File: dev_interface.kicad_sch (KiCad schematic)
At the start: 0 parts

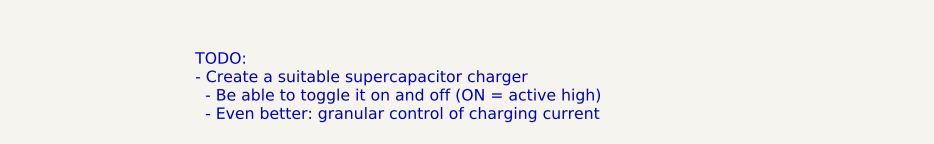
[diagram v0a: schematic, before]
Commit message: Added some text in the subsheets to outline what needs to be added inside of each subsheet
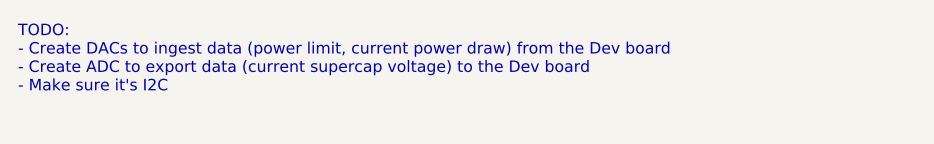
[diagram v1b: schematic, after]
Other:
- note added: "TODO: - Create DACs to ingest data (power limit, current power draw) from the Dev board - Create ADC to export data (current supercap voltage) to the Dev board - Make sure it's I2C"
- note removed: "TODO: - Create a suitable supercapacitor charger - Be able to toggle it on and off (ON = active high) - Even better: granular control of charging current"
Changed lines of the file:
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@@
 		(comment 1 "Robomaster")
 	)
-	(text "TODO:\n- Create a suitable supercapacitor charger\n  - Be able to toggle it on and off (ON = active high)\n  - Even better: granular control of charging current"
+	(text "TODO:\n- Create DACs to ingest data (power limit, current power draw) from the Dev board\n- Create ADC to export data (current supercap voltage) to the Dev board\n- Make sure it's I2C"
 		(exclude_from_sim no)
-		(at 132.08 95.25 0)
+		(at 112.395 92.075 0)
 		(effects
 			(font

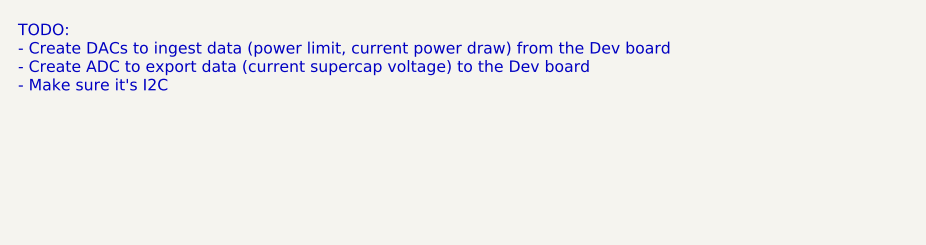
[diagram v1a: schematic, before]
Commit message: Added in & out data from each subsheet
For more details, please contact @leftisttachyon on Discord
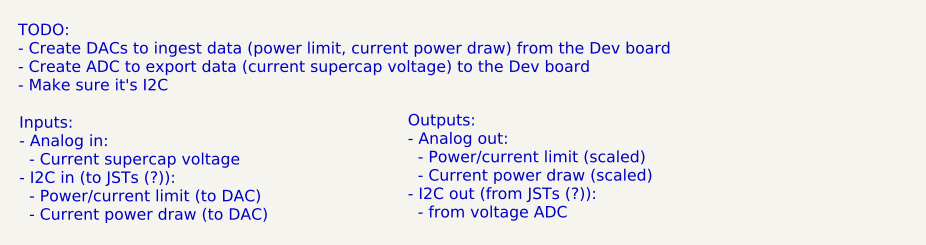
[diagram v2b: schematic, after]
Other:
- note added: "Inputs: - Analog in: - Current supercap voltage - I2C in (to JSTs (?)): - Power/current limit (to DAC) - Current power draw (to DAC)"
- note added: "Outputs: - Analog out: - Power/current limit (scaled) - Current power draw (scaled) - I2C out (from JSTs (?)): - from voltage ADC"
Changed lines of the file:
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@@
+		)
+	)
+	(text "Inputs:\n- Analog in:\n  - Current supercap voltage\n- I2C in (to JSTs (?)):\n  - Power/current limit (to DAC)\n  - Current power draw (to DAC)"
+		(exclude_from_sim no)
+		(at 112.522 102.362 0)
+		(effects
+			(font
+				(size 1.27 1.27)
+			)
+			(justify left top)
+		)
+	)
+	(text "Outputs:\n- Analog out:\n  - Power/current limit (scaled)\n  - Current power draw (scaled)\n- I2C out (from JSTs (?)):\n  - from voltage ADC"
+		(exclude_from_sim no)
+		(at 155.702 102.108 0)
+		(effects
+			(font
+				(size 1.27 1.27)
+			)
+			(justify left top)
 		)
 	)

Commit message: Completed first version of housekeeping supplies
+5V and +3V3 from mini PC +24V
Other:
- company: UT Stampede -> UT Robomaster
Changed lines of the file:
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@@
 	(paper "A4")
 	(title_block
-		(date "2024-10-18")
+		(date "2024-11-15")
 		(rev "1")
-		(company "UT Stampede")
+		(company "UT Robomaster")
 		(comment 1 "Robomaster")
 	)

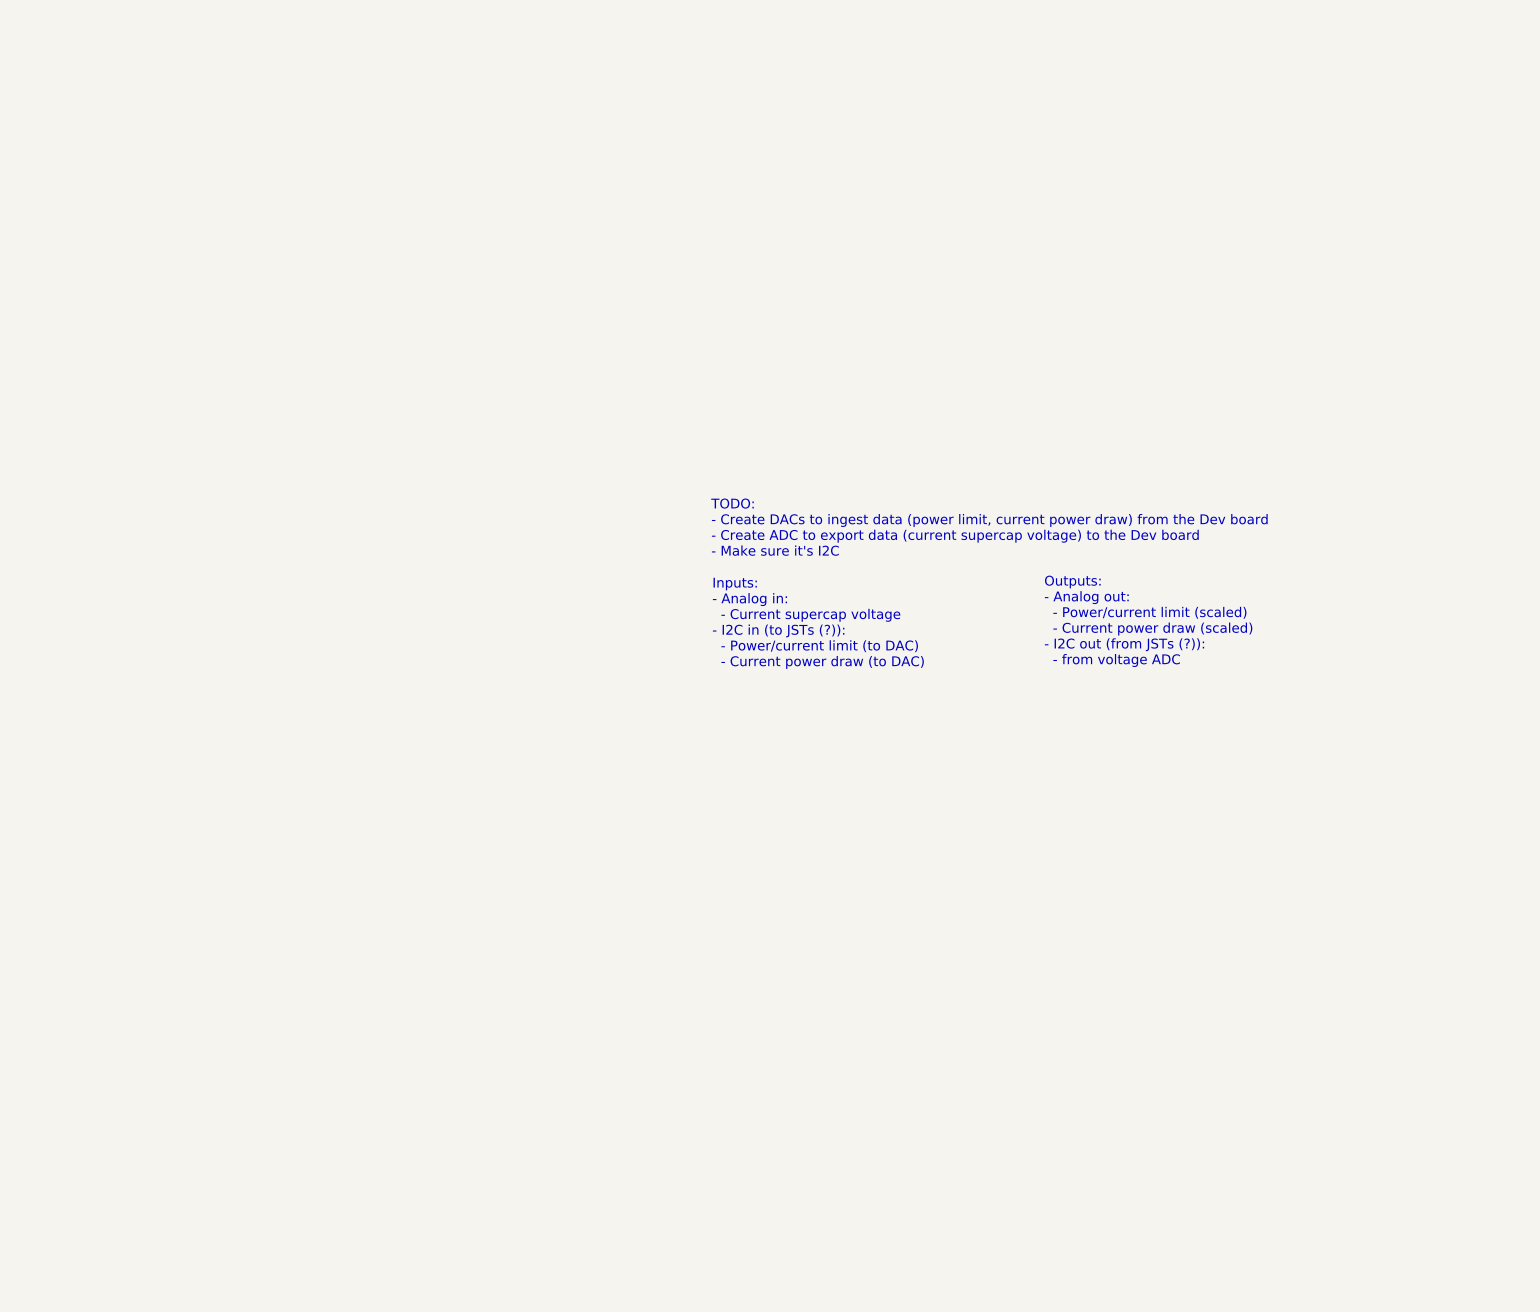
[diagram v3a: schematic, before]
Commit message: Selected an ideal diode
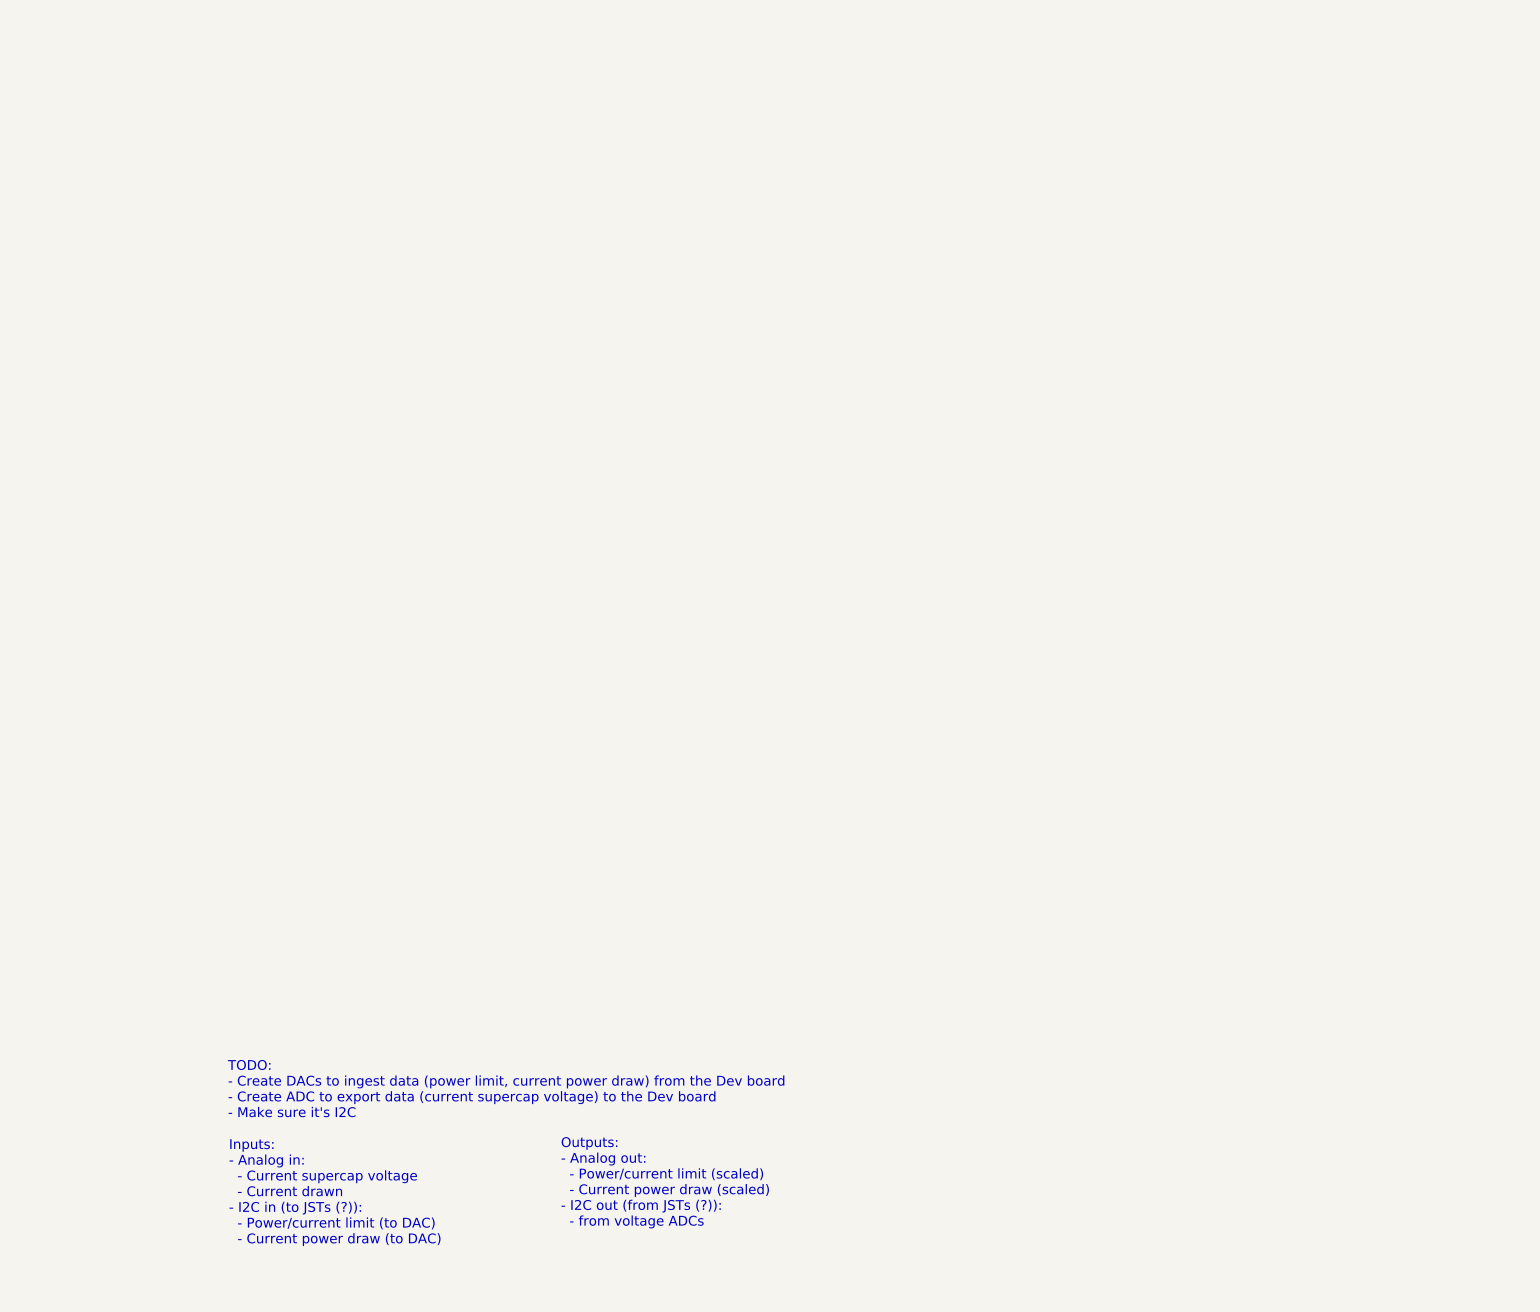
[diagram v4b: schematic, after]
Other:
- note added: "Inputs: - Analog in: - Current supercap voltage - Current drawn - I2C in (to JSTs (?)): - Power/current limit (to DAC) - Current power draw (to DAC)"
- note added: "Outputs: - Analog out: - Power/current limit (scaled) - Current power draw (scaled) - I2C out (from JSTs (?)): - from voltage ADCs"
- note removed: "Inputs: - Analog in: - Current supercap voltage - I2C in (to JSTs (?)): - Power/current limit (to DAC) - Current power draw (to DAC)"
- note removed: "Outputs: - Analog out: - Power/current limit (scaled) - Current power draw (scaled) - I2C out (from JSTs (?)): - from voltage ADC"
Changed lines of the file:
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@@
 	(text "TODO:\n- Create DACs to ingest data (power limit, current power draw) from the Dev board\n- Create ADC to export data (current supercap voltage) to the Dev board\n- Make sure it's I2C"
 		(exclude_from_sim no)
-		(at 112.395 92.075 0)
+		(at 49.53 165.1 0)
 		(effects
 			(font
@@
 		)
 	)
-	(text "Inputs:\n- Analog in:\n  - Current supercap voltage\n- I2C in (to JSTs (?)):\n  - Power/current limit (to DAC)\n  - Current power draw (to DAC)"
+	(text "Inputs:\n- Analog in:\n  - Current supercap voltage\n  - Current drawn\n- I2C in (to JSTs (?)):\n  - Power/current limit (to DAC)\n  - Current power draw (to DAC)"
 		(exclude_from_sim no)
-		(at 112.522 102.362 0)
+		(at 49.657 175.387 0)
 		(effects
 			(font
@@
 		)
 	)
-	(text "Outputs:\n- Analog out:\n  - Power/current limit (scaled)\n  - Current power draw (scaled)\n- I2C out (from JSTs (?)):\n  - from voltage ADC"
+	(text "Outputs:\n- Analog out:\n  - Power/current limit (scaled)\n  - Current power draw (scaled)\n- I2C out (from JSTs (?)):\n  - from voltage ADCs"
 		(exclude_from_sim no)
-		(at 155.702 102.108 0)
+		(at 92.837 175.133 0)
 		(effects
 			(font

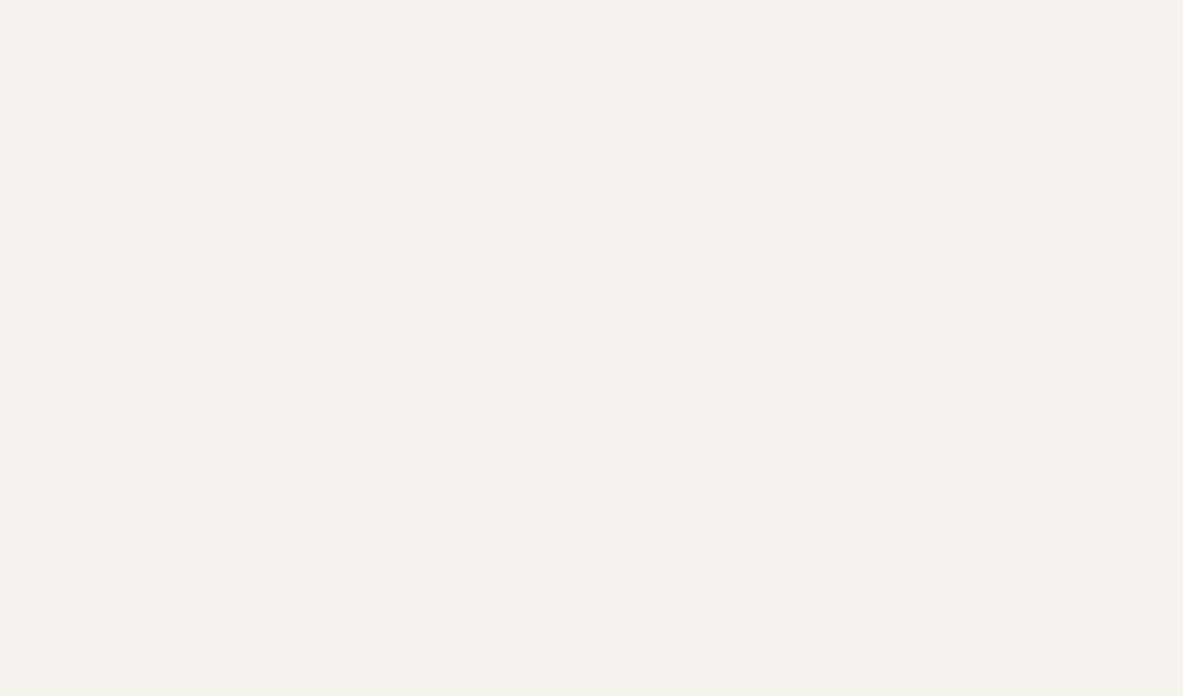
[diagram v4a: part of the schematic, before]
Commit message: Selected components for ideal diode and DACs
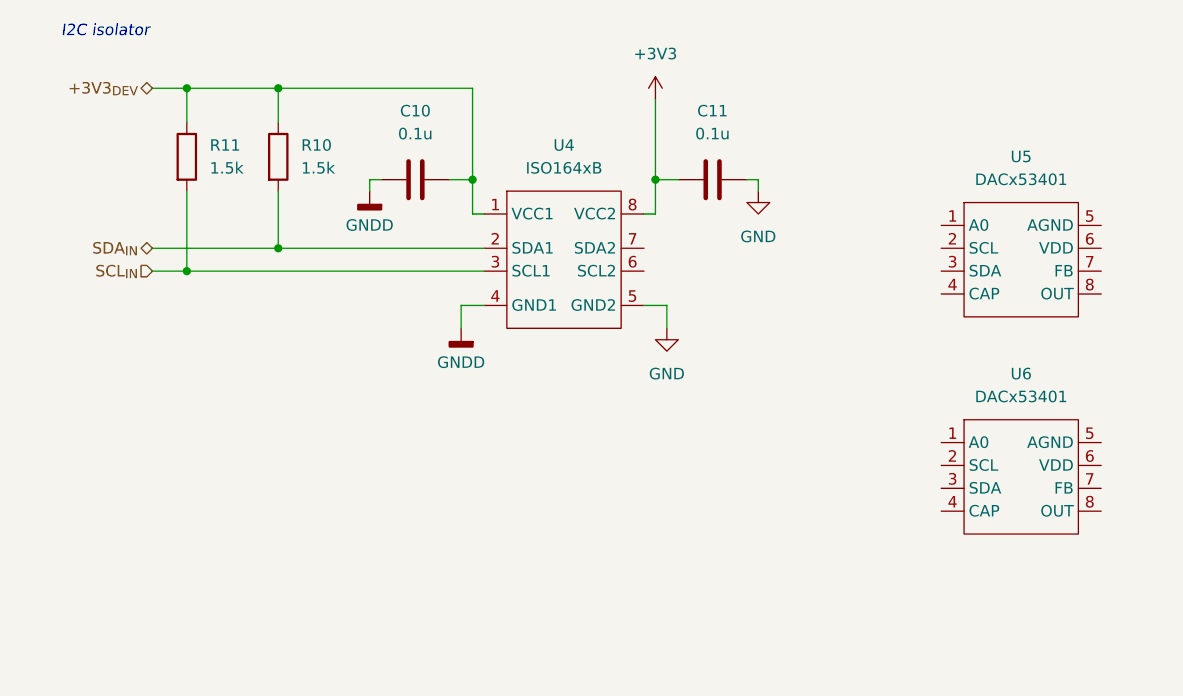
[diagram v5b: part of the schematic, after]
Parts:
- added C10, C11: 0.1u, Capacitor_SMD:C_0603_1608Metric_Pad1.08x0.95mm_HandSolder, symbol Device:C
- added R10, R11: 1.5k, Resistor_SMD:R_0603_1608Metric_Pad0.98x0.95mm_HandSolder, symbol Device:R
- added U4: ISO164xB, Package_SO:SOIC-8_3.9x4.9mm_P1.27mm, symbol ! Robomaster:ISO164xB
- added U5, U6: DACx53401, Package_SON:WSON-8-1EP_2x2mm_P0.5mm_EP0.9x1.6mm, symbol ! Robomaster:DACx3401
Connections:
- new net +3V3: C11.1, U4.8 (VCC2)
- new net +3V3_{DEV}: C10.2, R10.1, R11.1, U4.1 (VCC1)
- new net GND: C11.2, U4.5 (GND2)
- new net GNDD: C10.1, U4.4 (GND1)
- new net SCL_{IN}: R11.2, U4.3 (SCL1)
- new net SDA_{IN}: R10.2, U4.2 (SDA1)
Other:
- note added: "I2C isolator"

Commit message: Trying to do current sense but it's not fun
canercanercnarennc
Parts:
- added U8: LM2904, symbol Amplifier_Operational:LM2904
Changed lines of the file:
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@@
+	)
+	(symbol
+		(lib_id "Amplifier_Operational:LM2904")
+		(at 99.06 123.19 0)
+		(unit 3)
+		(exclude_from_sim no)
+		(in_bom yes)
+		(on_board yes)
+		(dnp no)
+		(fields_autoplaced yes)
+		(property "Reference" "U8"
+			(at 97.79 121.9199 0)
+			(effects
+				(font
+					(size 1.27 1.27)
+				)
+				(justify left)
+			)
+		)
+		(property "Value" "LM2904"
+			(at 97.79 124.4599 0)
+			(effects
+				(font
+					(size 1.27 1.27)
+				)
+				(justify left)
+			)
+		)
+		(property "Footprint" ""
+			(at 99.06 123.19 0)
+			(effects
+				(font
+					(size 1.27 1.27)
+				)
+				(hide yes)
+			)
+		)
+		(property "Datasheet" "http://www.ti.com/lit/ds/symlink/lm358.pdf"
+			(at 99.06 123.19 0)
+			(effects
+				(font
+					(size 1.27 1.27)
+				)
+				(hide yes)
+			)
+		)
+		(property "Description" "Dual Operational Amplifiers, DIP-8/SOIC-8/TSSOP-8/VSSOP-8"
+			(at 99.06 123.19 0)
+			(effects
+				(font
+					(size 1.27 1.27)
+				)
+				(hide yes)
+			)
+		)
+		(pin "1"
+		)
+		(pin "5"
+		)
+		(pin "6"
+		)
+		(pin "8"
+		)
+		(pin "3"
+		)
+		(pin "4"
+		)
+		(pin "2"
+		)
+		(pin "7"
+		)
+		(instances
+			(project "SupercapManager"
+				(path "/6197145b-e7d4-44cc-9d90-537b6501bf60/115b1a74-e36e-4ee6-8764-bf26e4e24147"
+					(reference "U8")
+					(unit 3)
+				)
+			)
+		)
 	)
 	(symbol
@@
 				)
 			)
+		)
+	)
+	(symbol
+		(lib_id "Amplifier_Operational:LM2904")
+		(at 101.6 99.06 0)
+		(unit 2)
+		(exclude_from_sim no)
+		(in_bom yes)
+		(on_board yes)
+		(dnp no)
+		(fields_autoplaced yes)
+		(property "Reference" "U8"
+			(at 101.6 88.9 0)
+			(effects
+				(font
+					(size 1.27 1.27)
+				)
+			)
+		)
+		(property "Value" "LM2904"
+			(at 101.6 91.44 0)
+			(effects
+				(font
+					(size 1.27 1.27)
+				)
+			)
+		)
+		(property "Footprint" ""
+			(at 101.6 99.06 0)
+			(effects
+				(font
+					(size 1.27 1.27)
+				)
+				(hide yes)
+			)
+		)
+		(property "Datasheet" "http://www.ti.com/lit/ds/symlink/lm358.pdf"
+			(at 101.6 99.06 0)
+			(effects
+				(font
+					(size 1.27 1.27)
+				)
+				(hide yes)
+			)
+		)
+		(property "Description" "Dual Operational Amplifiers, DIP-8/SOIC-8/TSSOP-8/VSSOP-8"
+			(at 101.6 99.06 0)
+			(effects
+				(font
+					(size 1.27 1.27)
+				)
+				(hide yes)
+			)
+		)
+		(pin "5"
+		)
+		(pin "4"
+		)
+		(pin "8"
+		)
+		(pin "1"
+		)
+		(pin "6"
+		)
+		(pin "3"
+		)
+		(pin "7"
+		)
+		(pin "2"
+		)
+		(instances
+			(project "SupercapManager"
+				(path "/6197145b-e7d4-44cc-9d90-537b6501bf60/115b1a74-e36e-4ee6-8764-bf26e4e24147"
+					(reference "U8")
+					(unit 2)
+				)
+			)

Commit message: Finish Dev board interface
sorry morris
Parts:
- added C12, C13: 6.8u, Capacitor_SMD:C_0603_1608Metric_Pad1.08x0.95mm_HandSolder, symbol Device:C
- added C14, C15, C16, C17, C18: 0.1u, symbol Device:C
- added U10, U11: ADS1014IDGS, Package_SO:TSSOP-10_3x3mm_P0.5mm, symbol Analog_ADC:ADS1014IDGS
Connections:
- net +3V3: now also U5.1 (A0), U5.6 (VDD), U6.6 (VDD), U8.8 (V+), C14.2, C15.2, C16.2, C17.2, C18.2, U10.8 (VDD), U11.1 (ADDR), U11.8 (VDD)
- net GND: now also U5.5 (AGND), U6.1 (A0), U6.5 (AGND), U8.4 (V-), C12.2, C13.2, C14.1, C15.1, C16.1, C17.1, C18.1, U10.1 (ADDR), U10.3 (GND), U10.5 (AIN1), U11.3 (GND), U11.5 (AIN1)
- net SCL_{INT}: now reaches U5.2 (SCL)
- net SCL_{INT}: now also U4.7 (SDA2), U6.2 (SCL), U10.10 (SCL), U11.10 (SCL)
- net SDA_{INT}: now reaches U5.3 (SDA)
- net SDA_{INT}: now also U4.6 (SCL2), U6.3 (SDA), U10.9 (SDA), U11.9 (SDA)
- net CAP_{1}: now reaches U5.4 (CAP)
- net CAP_{1}: now also C13.1
- net DAC_{1}_FB: now reaches U5.7 (FB)
- net POW_LIMIT: now reaches U5.8 (OUT)
- net CAP_{2}: now reaches U6.4 (CAP)
- net CAP_{2}: now also C12.1
- net DAC_{2}_FB: now reaches U6.7 (FB)
- net POW_DRAW: now reaches U6.8 (OUT)
- net V_{SC}: now reaches U8.5 (+)
- net V_{SC}_BUF: now reaches U8.6 (-)
- net V_{SC}_BUF: now also U8.7, U11.4 (AIN0)
- new net CURR: U10.4 (AIN0)
- no-connect marks 0 -> 2
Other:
- note added: "ADC_{1} ADDR: 1001000R_{2}"
- note added: "ADC_{2} ADDR: 1001001R_{2}"
- note added: "Analog buffering (V_{CAP})"
- note added: "Analog-to-digital converters (ADCs)"
- note added: "DAC_{1} ADDR: 1001001R_{2}"
- note added: "DAC_{2} ADDR: 1001000R_{2}"
- note added: "Digital-to-analog converters (DACs)"
- moved on the sheet: U5, U6, U8B, U8C
